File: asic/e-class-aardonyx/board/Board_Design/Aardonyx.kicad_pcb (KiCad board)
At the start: 2 copper layers, 298 parts, among them J1 USB_B_6PIN, J10 Conn_1x6_F, J11 Conn_1x6_F, J12 Conn_1x3_M, J13 Conn_1x8_F, J14 Conn_1x6_F, J15 Conn_1x10, J16 Conn_1x8_F, J17 USB_OTG, J18 Conn_1x3_M, J19 Conn_1x3_M, J2 Conn_1x8, J3 Conn_1x3_M, J4 Conn_1x4, J5 PJ-202H PWRJACK, J6 Conn_1x3_M, J7 Conn_1x4, J8 Conn_1x3_M, J9 Conn_1x8, Q1 FDN339AN, SW1 SW_SPST, SW2 FSM2JSMAATR, SW3 SW_DIP_x03, U1 FT2232H, U10 TPS7A7002DDAR, U11 ADM1085, U12 ADM1085, U13 TPS7A7002DDAR, U14 74AUP1G09GW, U15 SKT32E, U16 93LC56BT-I_OT, U2 IS42S32160F-TSOP2, U3 CDCE913PW, U4 TPS54627DDAR, U5 CAT24M01WI-GT3, U6 IS25LP256x-xM, U7 ADC108S102CIMTX, U8 LSF0108PWR, U9 LSF0108PWR, Y1 12MHz, Y2 27MHz

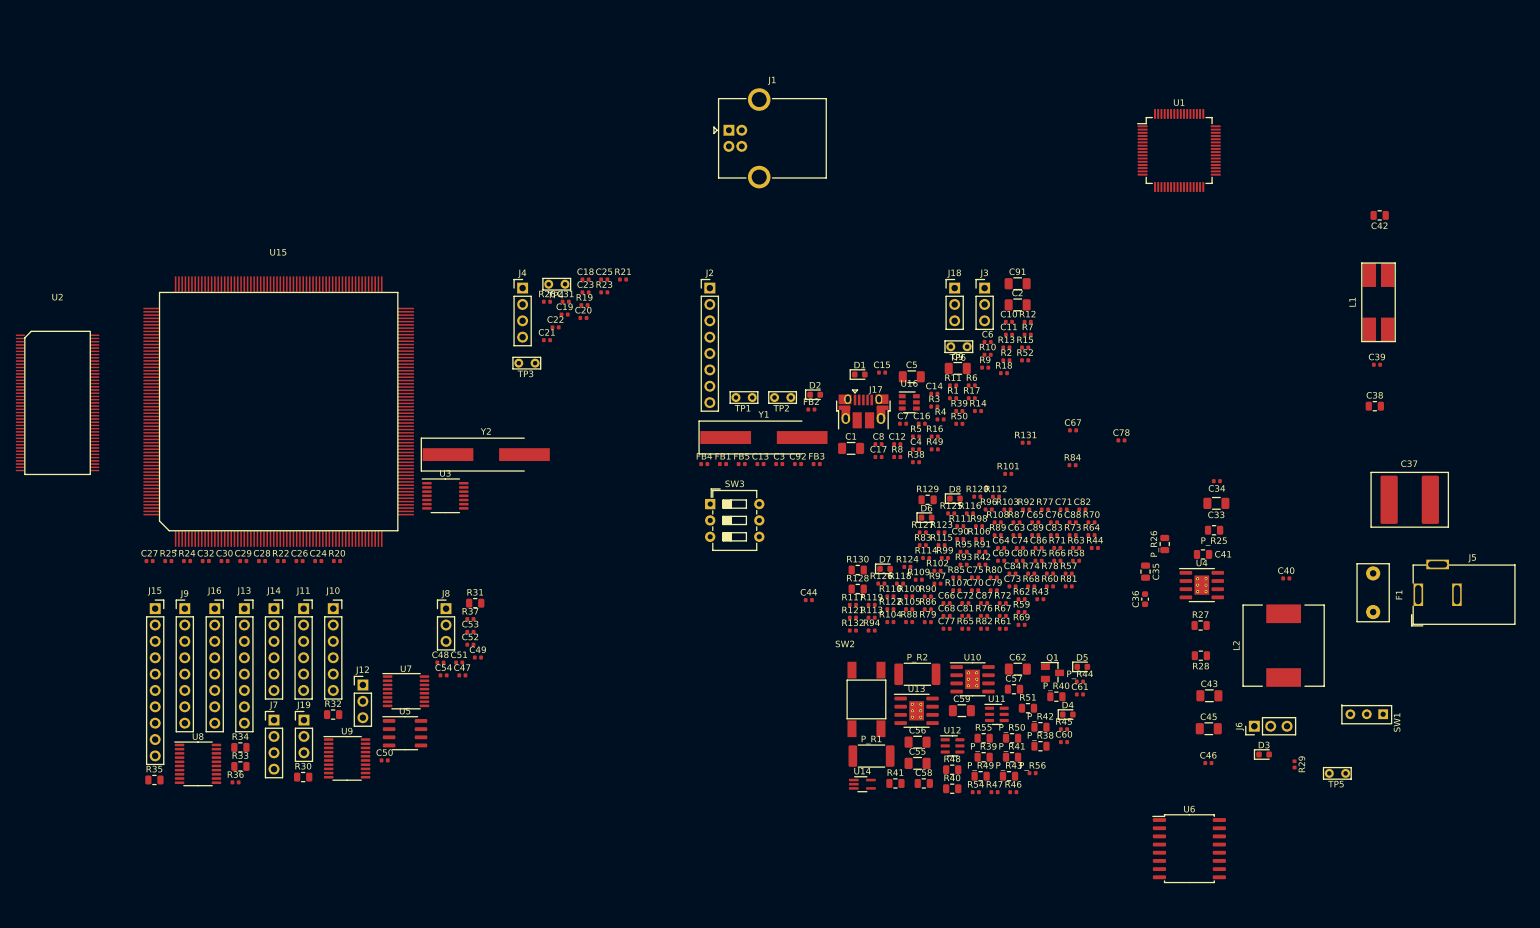
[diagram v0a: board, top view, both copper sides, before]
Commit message: update pec & footprint
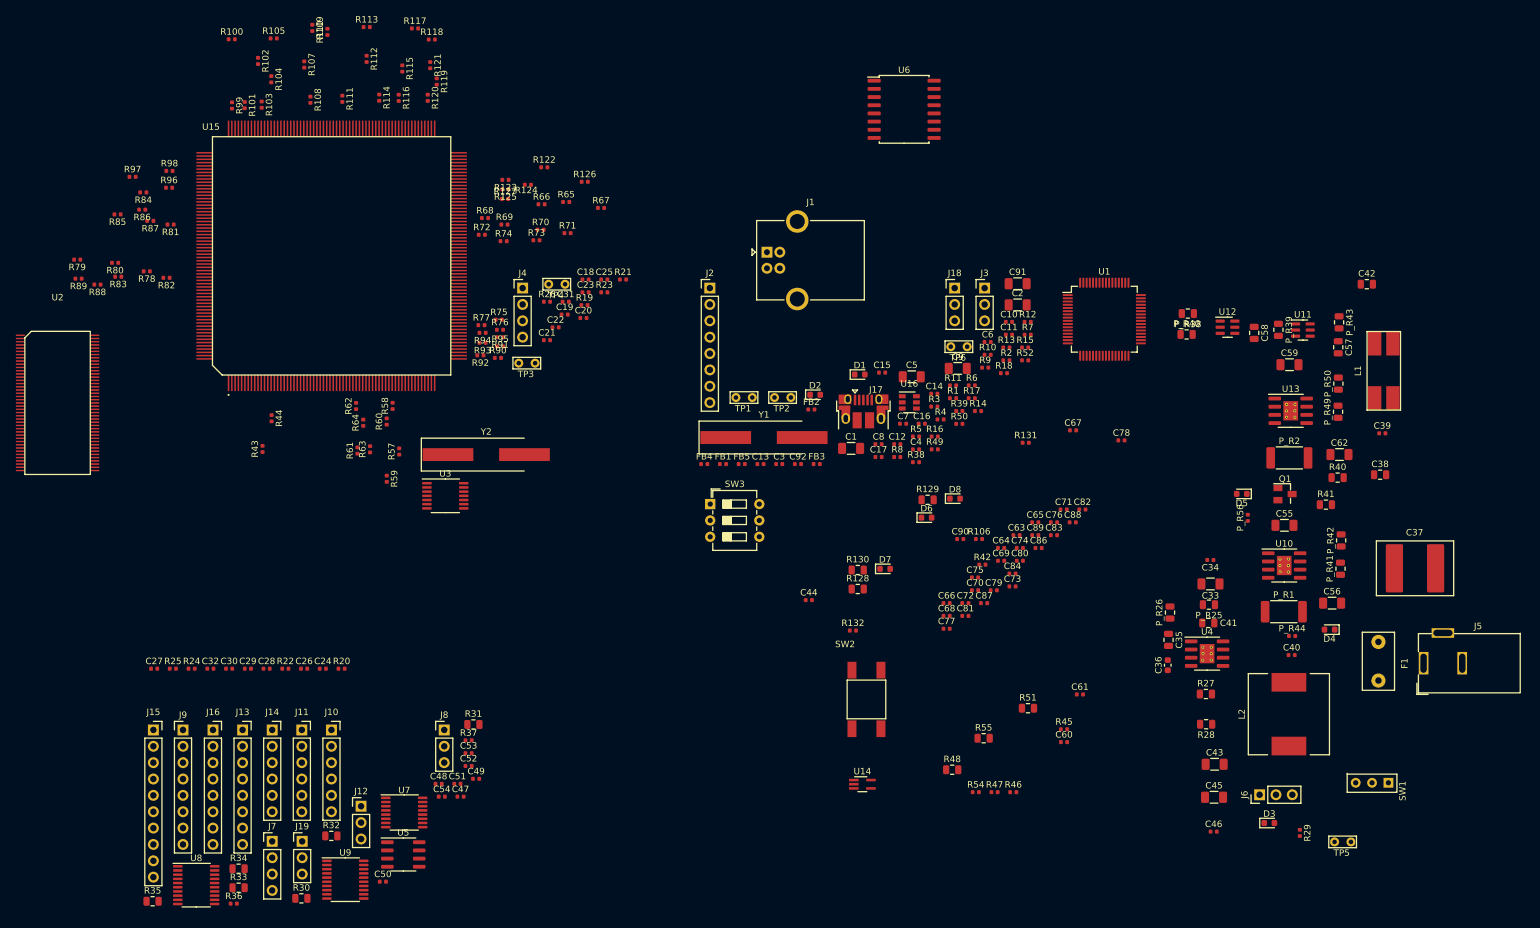
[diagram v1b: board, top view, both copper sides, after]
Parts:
- moved R84 150.4 mm to (53.2, 51.7), turned to 180 degrees
- moved R81 150.3 mm to (57.5, 56.7), turned to 180 degrees
- moved R89 148.2 mm to (43.2, 65.1), turned to 180 degrees
- moved R78 147.9 mm to (53.8, 64.0), turned to 180 degrees
- moved R80 144.9 mm to (48.9, 62.6), turned to 180 degrees
- moved R79 143.6 mm to (43.0, 62.2), turned to 180 degrees
- moved R87 142.4 mm to (54.3, 56.1), turned to 180 degrees
- moved R85 141.9 mm to (49.2, 55.1), turned to 180 degrees
- moved R97 140.0 mm to (51.6, 49.3)
- moved R82 138.1 mm to (56.8, 65.0), turned to 180 degrees
- moved R98 137.3 mm to (57.3, 48.4)
- moved R86 136.9 mm to (53.1, 54.4), turned to 180 degrees
- moved R96 136.7 mm to (57.2, 51.0)
- moved R88 136.5 mm to (46.1, 66.0), turned to 180 degrees
- moved R100 136.2 mm to (67.0, 27.9)
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
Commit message: update component placement
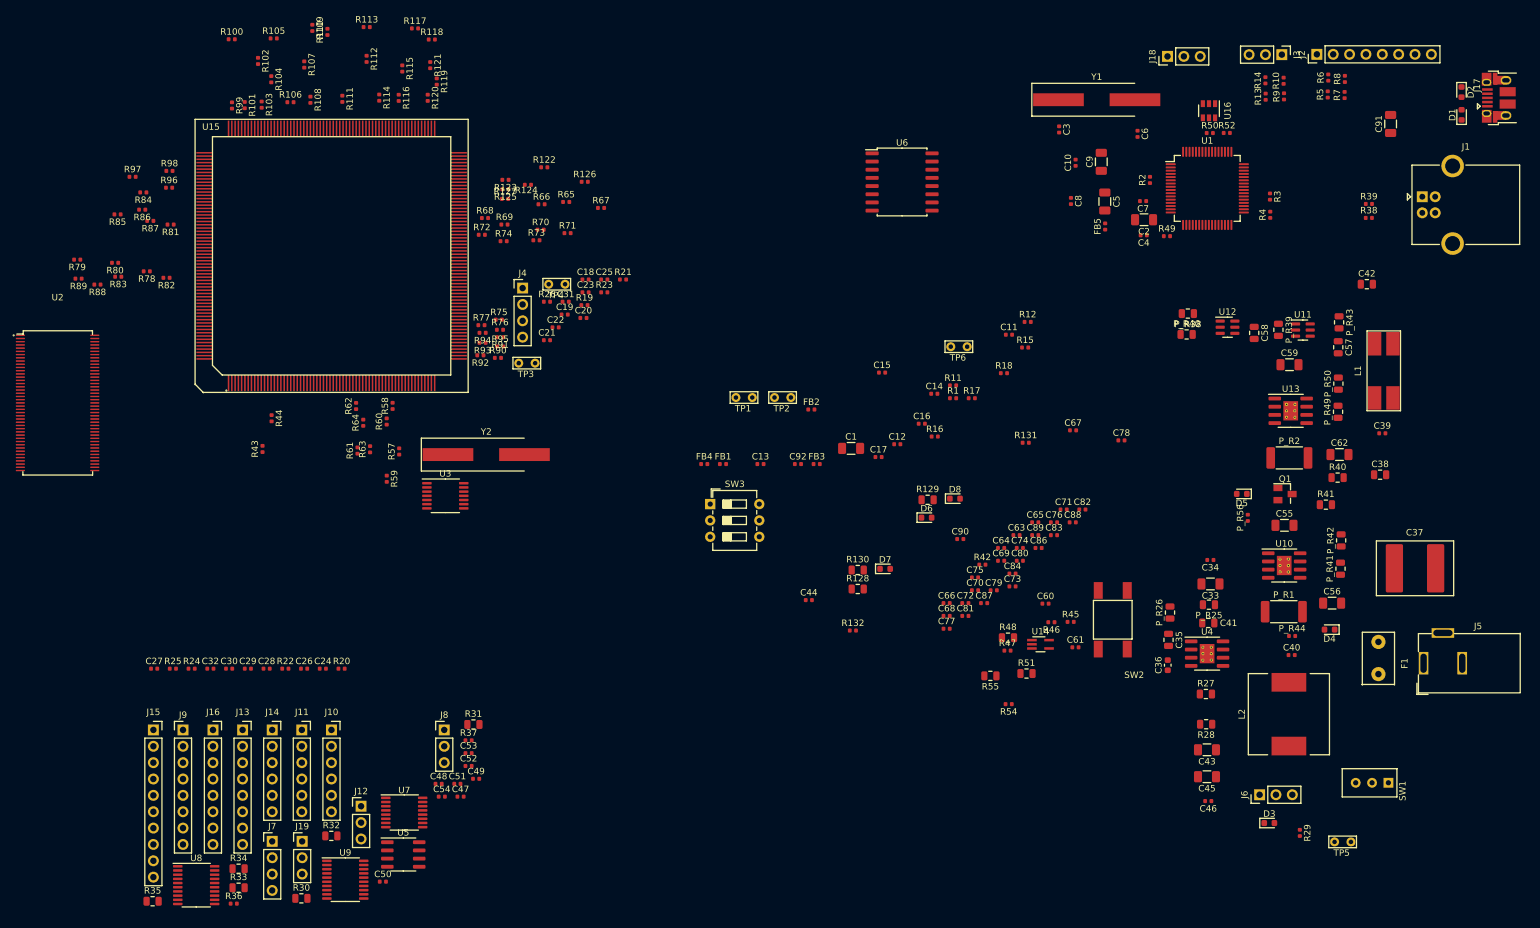
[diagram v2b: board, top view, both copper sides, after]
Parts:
- moved R106 126.6 mm to (76.1, 37.7)
- moved D2 110.8 mm to (257.9, 36.1), turned to 270 degrees
- moved J17 110.0 mm to (263.7, 37.0), turned to 90 degrees
- moved J1 102.1 mm to (251.8, 52.4)
- moved D1 101.8 mm to (257.9, 39.7), turned to 90 degrees
- moved J2 101.0 mm to (235.4, 30.3), turned to 90 degrees
- moved R8 91.0 mm to (239.8, 34.1), turned to 90 degrees
- moved R5 83.1 mm to (237.1, 36.5), turned to 90 degrees
- moved R38 79.9 mm to (243.5, 55.7)
- moved Y1 73.6 mm to (201.3, 37.3)
- moved R6 73.1 mm to (237.2, 33.9), turned to 90 degrees
- moved R39 71.3 mm to (243.5, 53.5)
- moved R14 68.0 mm to (227.4, 34.3), turned to 90 degrees
- moved C3 67.7 mm to (195.4, 41.9), turned to 270 degrees
- moved FB5 67.4 mm to (202.6, 57.0), turned to 90 degrees
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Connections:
- J3 pad 2: /ftdi/UART0_RX -> /ftdi/UART0_TX
- R13 pad 2: /ftdi/UART0_RX -> /ftdi/UART0_TX
- R14 pad 1: /ftdi/UART0_RX -> /ftdi/UART0_TX
- R4 pad 2: /ftdi/UART0_RX -> /ftdi/UART0_TX
- U15 pad 18: /ftdi/UART0_RX -> /ftdi/UART0_TX

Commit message: update foot print & componenet placement
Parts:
- Y1, Y2: footprint Crystal:Crystal_SMD_HC49-SD_HandSoldering -> Aardonyx:Crystal_SMD_ROHS_CSM_7XDN_HandSoldering
- moved U6 145.4 mm to (41.2, 115.6)
- moved FB4 111.4 mm to (243.6, 52.0), turned to 180 degrees
- moved C13 95.5 mm to (232.8, 48.1), turned to 90 degrees
- moved R16 88.9 mm to (245.4, 34.0), turned to 90 degrees
- moved R104 88.2 mm to (158.8, 54.9)
- moved R110 88.2 mm to (167.5, 47.6)
- moved R111 88.2 mm to (169.8, 58.0)
- moved R115 88.2 mm to (179.1, 53.3)
- moved R117 88.2 mm to (181.1, 47.0)
- moved R58 88.2 mm to (177.6, 105.6)
- moved R63 88.2 mm to (174.1, 112.4)
- moved R64 88.2 mm to (173.1, 108.3)
- moved R71 88.2 mm to (204.8, 78.8)
- moved R75 88.2 mm to (194.1, 92.3)
- moved R80 88.2 mm to (134.5, 83.4)
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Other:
- copper layers 2 -> 4

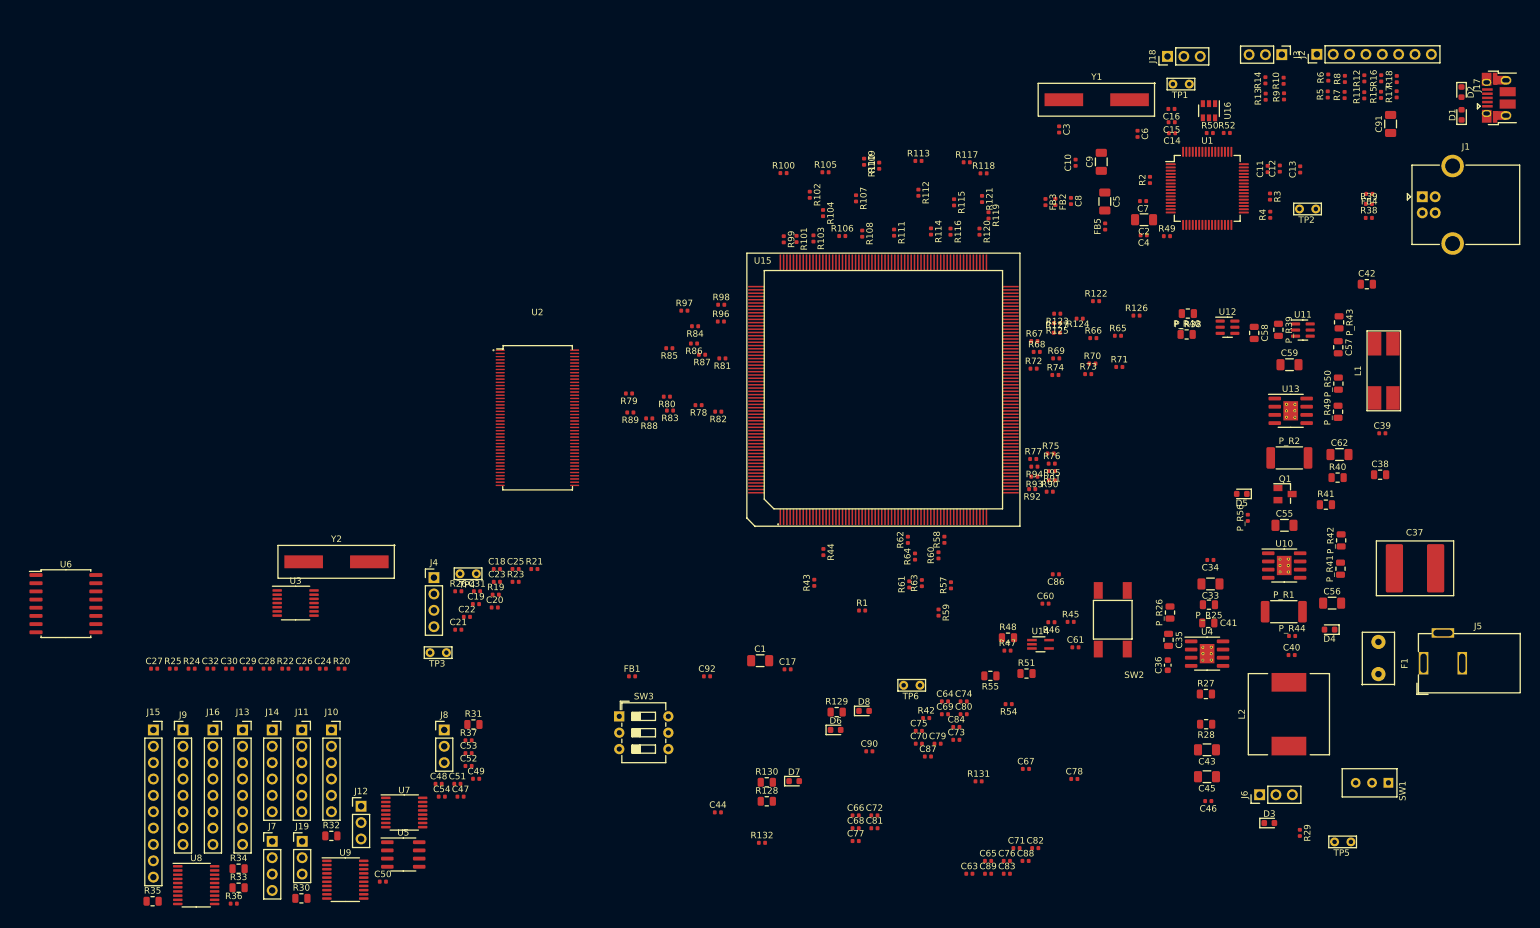
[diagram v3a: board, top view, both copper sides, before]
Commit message: update footprint & component placement
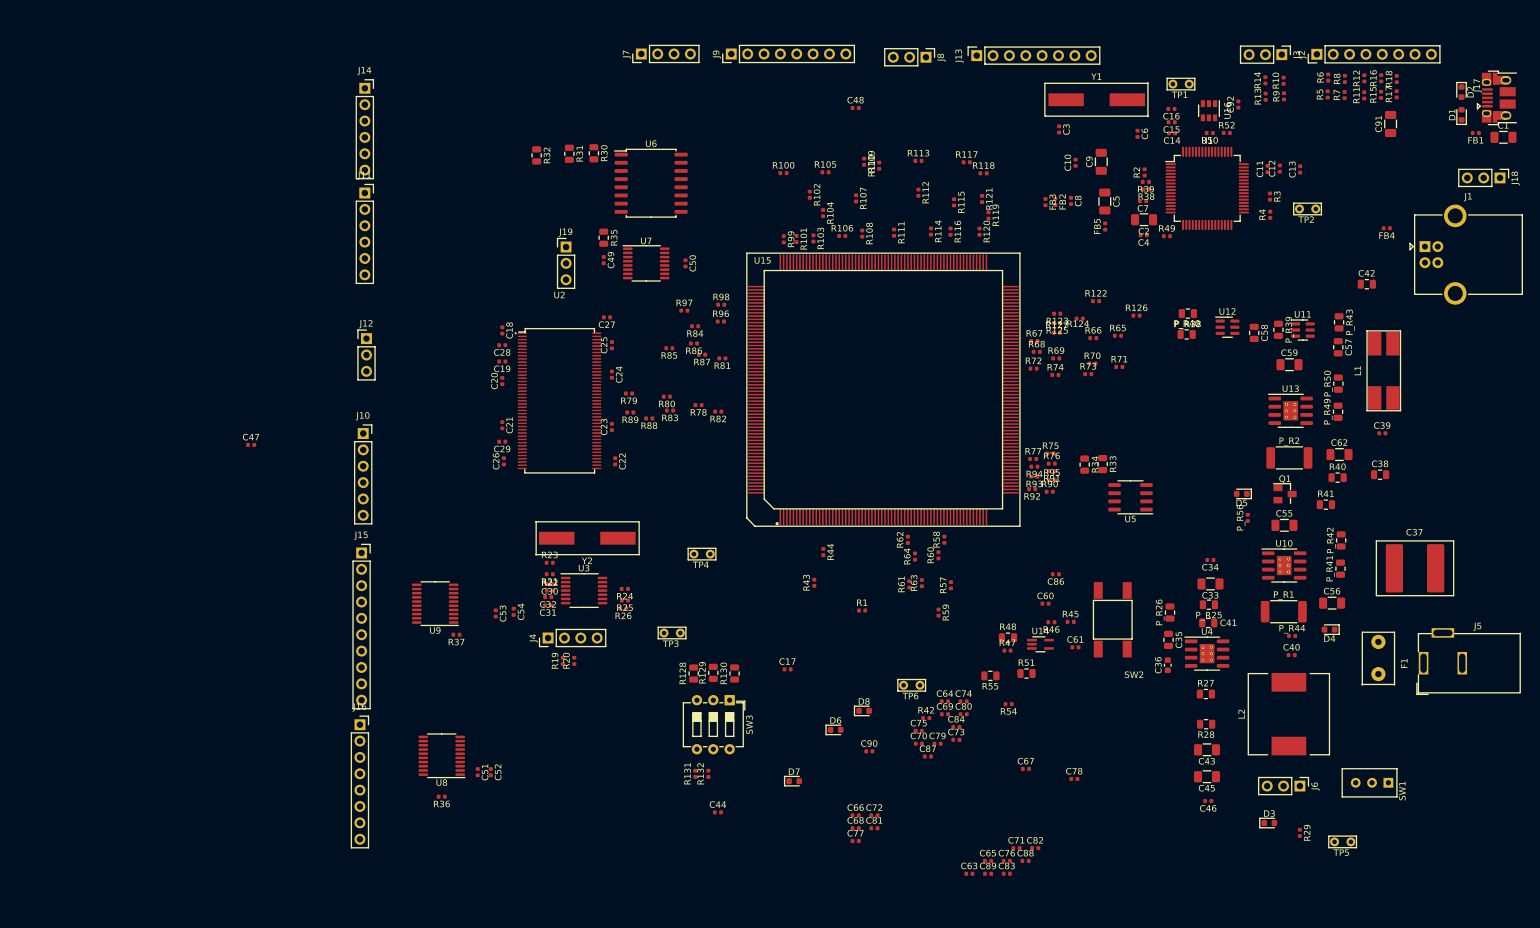
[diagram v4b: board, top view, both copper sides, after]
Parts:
- moved FB1 155.8 mm to (260.1, 42.5), turned to 180 degrees
- moved J13 154.8 mm to (182.6, 30.5), turned to 90 degrees
- moved R33 149.4 mm to (202.2, 93.9), turned to 270 degrees
- moved R34 145.6 mm to (199.4, 94.0), turned to 270 degrees
- moved C1 141.1 mm to (264.4, 43.2)
- moved J9 135.1 mm to (144.5, 30.2), turned to 90 degrees
- moved J7 135.0 mm to (130.6, 30.2), turned to 90 degrees
- moved J8 128.5 mm to (174.8, 30.7), turned to 270 degrees
- moved U5 125.8 mm to (206.5, 99.1), turned to 180 degrees
- moved R35 124.6 mm to (124.7, 58.8), turned to 270 degrees
- moved R30 124.3 mm to (123.2, 45.6), turned to 270 degrees
- moved C48 123.3 mm to (163.8, 38.6)
- moved C92 121.2 mm to (223.2, 38.1), turned to 90 degrees
- moved U6 111.9 mm to (132.1, 50.3)
- moved R32 110.4 mm to (114.3, 46.0), turned to 270 degrees
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
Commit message: update component palcement comment by kottee
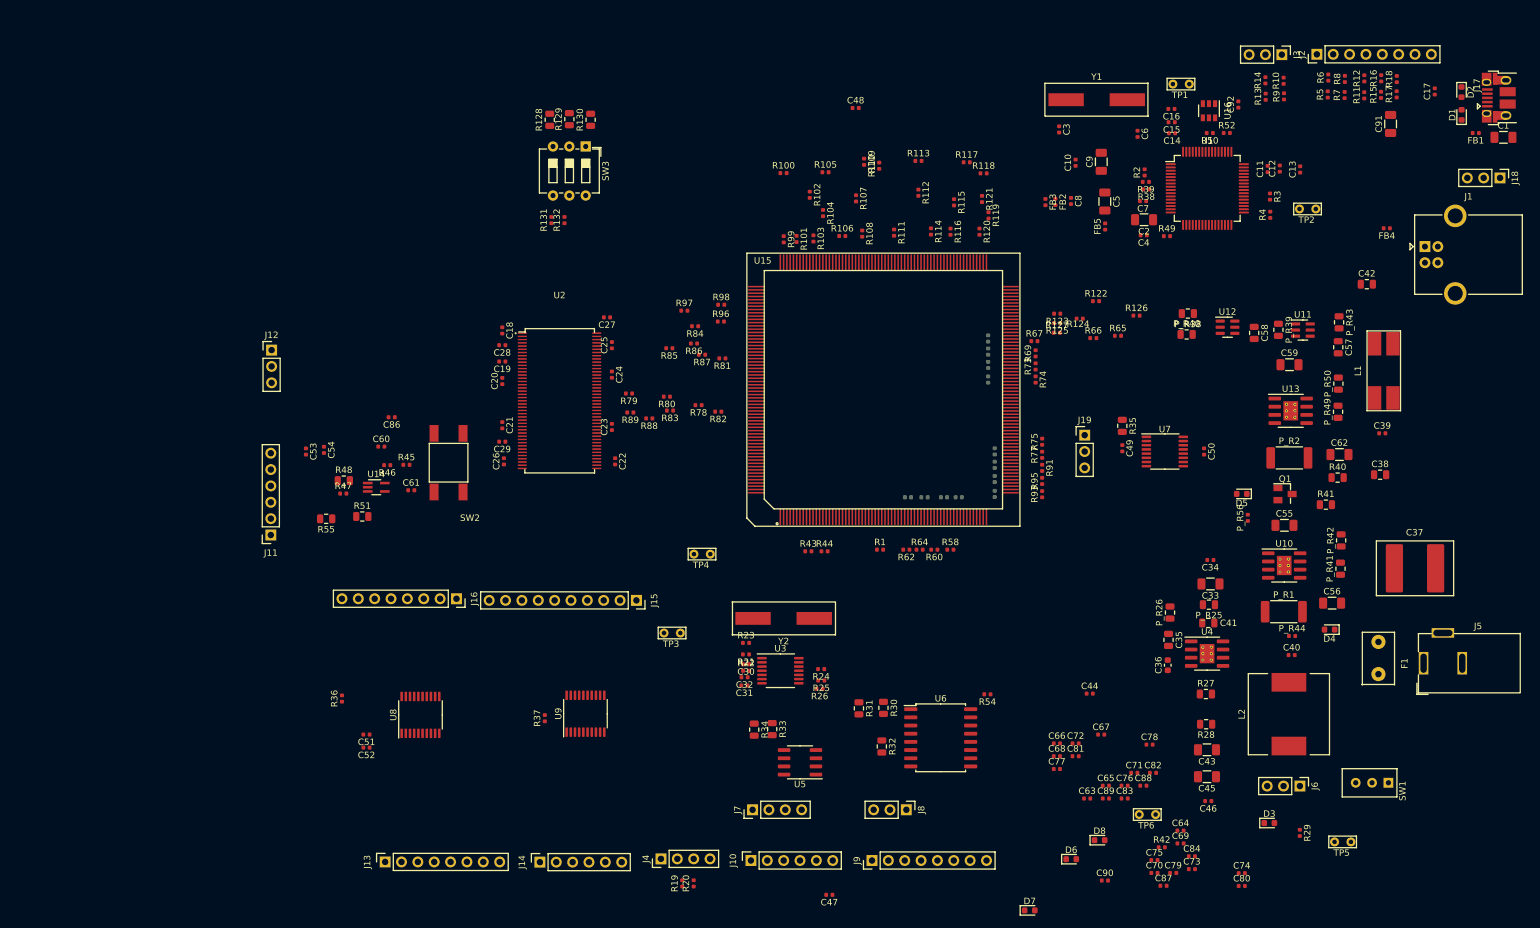
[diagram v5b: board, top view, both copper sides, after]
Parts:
- R57, R59, R61, R63, R68, R70, R71, R72, R76, R90, R92, R94: moved to B.Cu
- moved J13 155.3 mm to (90.8, 155.7)
- moved C17 134.7 mm to (253.7, 36.0), turned to 90 degrees
- moved J9 127.1 mm to (166.4, 155.4)
- moved J14 123.2 mm to (114.8, 155.7), turned to 90 degrees
- moved J7 118.6 mm to (147.8, 147.6)
- moved J8 116.9 mm to (171.7, 147.6)
- moved C47 113.7 mm to (159.7, 160.8), turned to 180 degrees
- moved R32 106.3 mm to (167.9, 137.7)
- moved C61 106.0 mm to (94.8, 98.0)
- moved R45 106.0 mm to (94.1, 94.0)
- moved C60 106.0 mm to (90.2, 91.2)
- moved R46 106.0 mm to (91.1, 94.1)
- moved R47 106.0 mm to (84.3, 98.5)
- moved R55 106.0 mm to (81.6, 102.4)
- moved SW2 106.0 mm to (100.6, 93.7)
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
